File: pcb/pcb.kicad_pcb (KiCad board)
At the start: 2 copper layers, 130.9 x 223.4 mm, 44 parts, among them J1 GPS Module Breakout, J2 MicroSD Card Breakout, U1 XIAO-ESP32-C5-DIP, U10 XIAO-ESP32-C5-DIP, U11 XIAO-ESP32-C5-DIP, U12 XIAO-ESP32-C5-DIP, U13 XIAO-ESP32-C5-DIP, U14 XIAO-ESP32-C5-DIP, U15 XIAO-ESP32-C5-DIP, U16 XIAO-ESP32-C5-DIP, U17 ESP32-S3 DevKitC-1, U18 LD1117V33, U19 SN74HC125N, U2 XIAO-ESP32-C5-DIP, U20 SN74HC138N, U21 SN74HC138N, U3 XIAO-ESP32-C5-DIP, U4 XIAO-ESP32-C5-DIP, U5 XIAO-ESP32-C5-DIP, U6 XIAO-ESP32-C5-DIP, U7 XIAO-ESP32-C5-DIP, U8 XIAO-ESP32-C5-DIP, U9 XIAO-ESP32-C5-DIP

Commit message: implement more feedback from red :D
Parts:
- moved C2 5.35 mm to (68.4, 97.5), turned to 0 degrees
- moved R1 3.91 mm to (66.4, 120.5)
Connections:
- C2 pad 1: /CS 00 -> Net-(J2-Pin_6)
- J2 pad 6: /CS 00 -> Net-(J2-Pin_6)
- R1 pad 1: /CS 00 -> Net-(J2-Pin_6)
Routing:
- net +5V: track 0.00 -> 365.9 mm
- net GND: track 0.00 -> 365.6 mm
- net /MOSI: track 0.00 -> 240.4 mm
- net /MISO: track 0.00 -> 235.9 mm
- net /SCK: track 0.00 -> 232.9 mm
- net /CS 01: track 0.00 -> 145.0 mm
- net /CS 02: track 0.00 -> 117.6 mm
- net /CS 08: track 0.00 -> 110.9 mm
- net /CS 03: track 0.00 -> 91.0 mm
- net /CS 07: track 0.00 -> 90.7 mm
- net /CS 06: track 0.00 -> 67.2 mm
- net /CS 04: track 0.00 -> 63.7 mm
- net /CS 05: track 0.00 -> 55.5 mm
- net Net-(U18-VO): track 0.00 -> 41.9 mm
- net /CS 00: track 0.00 -> 37.5 mm
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- added copper zone on F.Cu, net GND

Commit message: Reroute the board!
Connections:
- C2 pad 1: Net-(J2-Pin_6) -> +3.3V
- C2 pad 2: Net-(U18-VO) -> GND
- C3 pad 2: Net-(U18-VO) -> +3.3V
- J2 pad 1: Net-(J2-Pin_1) -> /CS 00
- J2 pad 6: Net-(J2-Pin_6) -> +3.3V
- R1 pad 1: Net-(J2-Pin_6) -> +3.3V
- U18 pad 2: Net-(U18-VO) -> +3.3V
- U19 pad 11: Net-(J2-Pin_1) -> unconnected-(U19-4Y-Pad11)
- U19 pad 12: /CS 00 -> GND
- U19 pad 14: Net-(U18-VO) -> +3.3V
- U20 pad 16: +5V -> +3.3V
- U20 pad 6: +5V -> +3.3V
- U21 pad 16: +5V -> +3.3V
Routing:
- net /MOSI: track 240.4 -> 604.1 mm, vias 0 -> 5
- net /MISO: track 235.9 -> 582.3 mm, vias 0 -> 3
- net /SCK: track 232.9 -> 578.6 mm, vias 0 -> 3
- net +5V: track 365.9 -> 645.8 mm
- net GND: track 365.6 -> 515.0 mm
- net /CS 09: track 0.00 -> 141.6 mm
- net +3.3V: track 0.00 -> 138.3 mm, vias 0 -> 3
- net /GPS_TX: track 0.00 -> 132.3 mm
- net /GPS_RX: track 0.00 -> 126.1 mm
- net /CS 15: track 0.00 -> 119.7 mm
- net /CS 10: track 0.00 -> 112.0 mm
- net /CS 11: track 0.00 -> 90.9 mm
- net /CS 16: track 0.00 -> 84.7 mm
- net /CS 00: track 37.5 -> 115.6 mm
- net /CS Addr 1: track 0.00 -> 77.4 mm
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
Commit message: Add brownout protection
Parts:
- added C4: 47uF, Capacitor_THT:C_Disc_D5.0mm_W2.5mm_P2.50mm, F.Cu at (76.5, 17.0)
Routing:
- net +5V: track 645.8 -> 650.1 mm

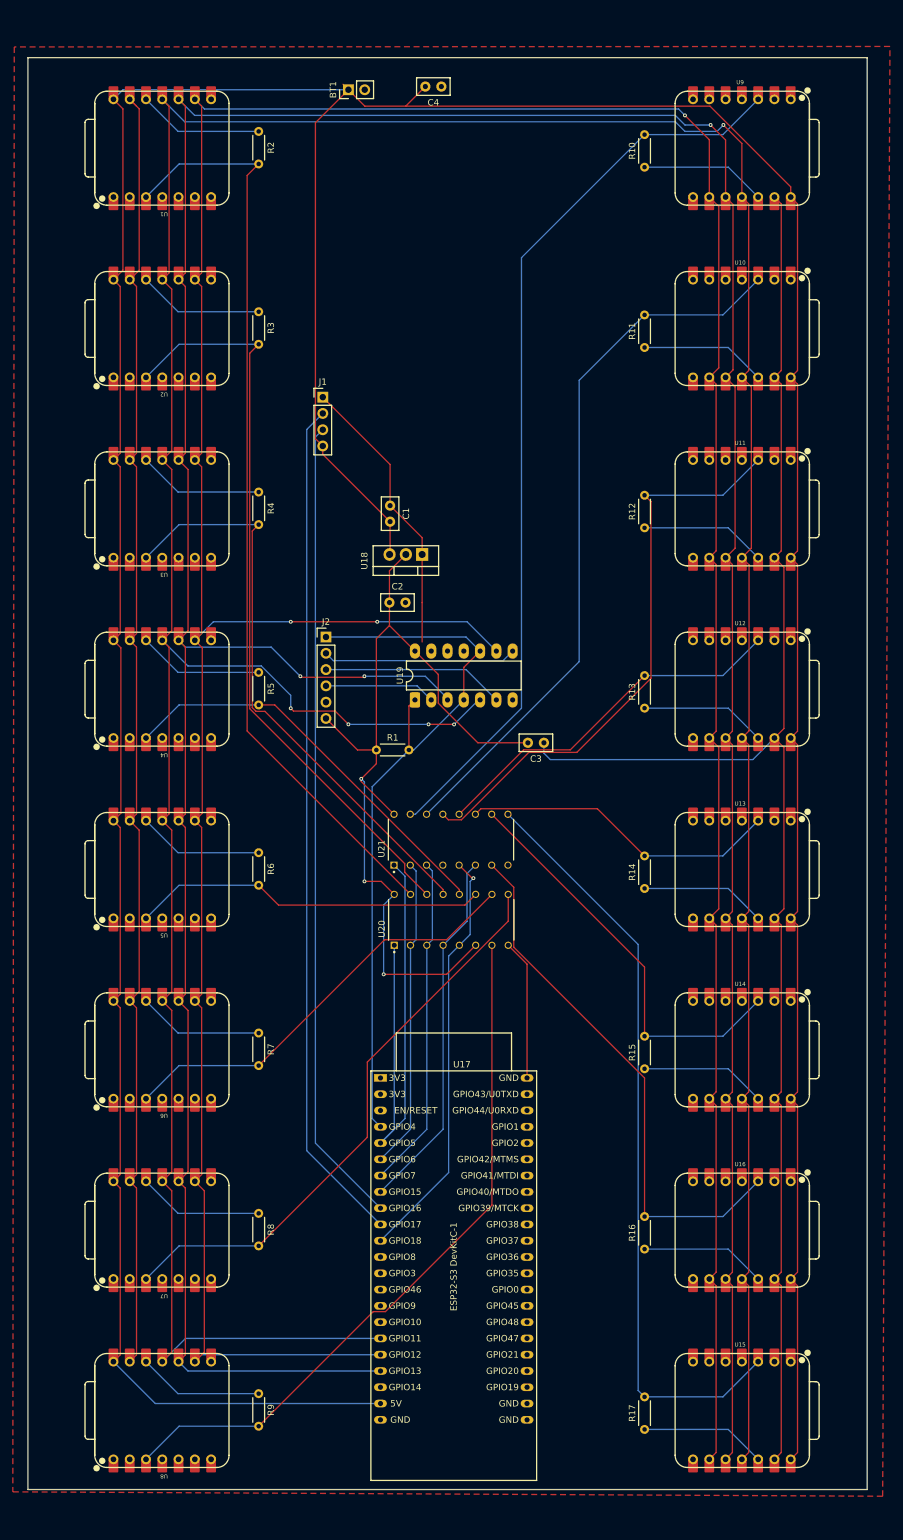
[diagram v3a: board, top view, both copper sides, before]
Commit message: 0.3mm power net
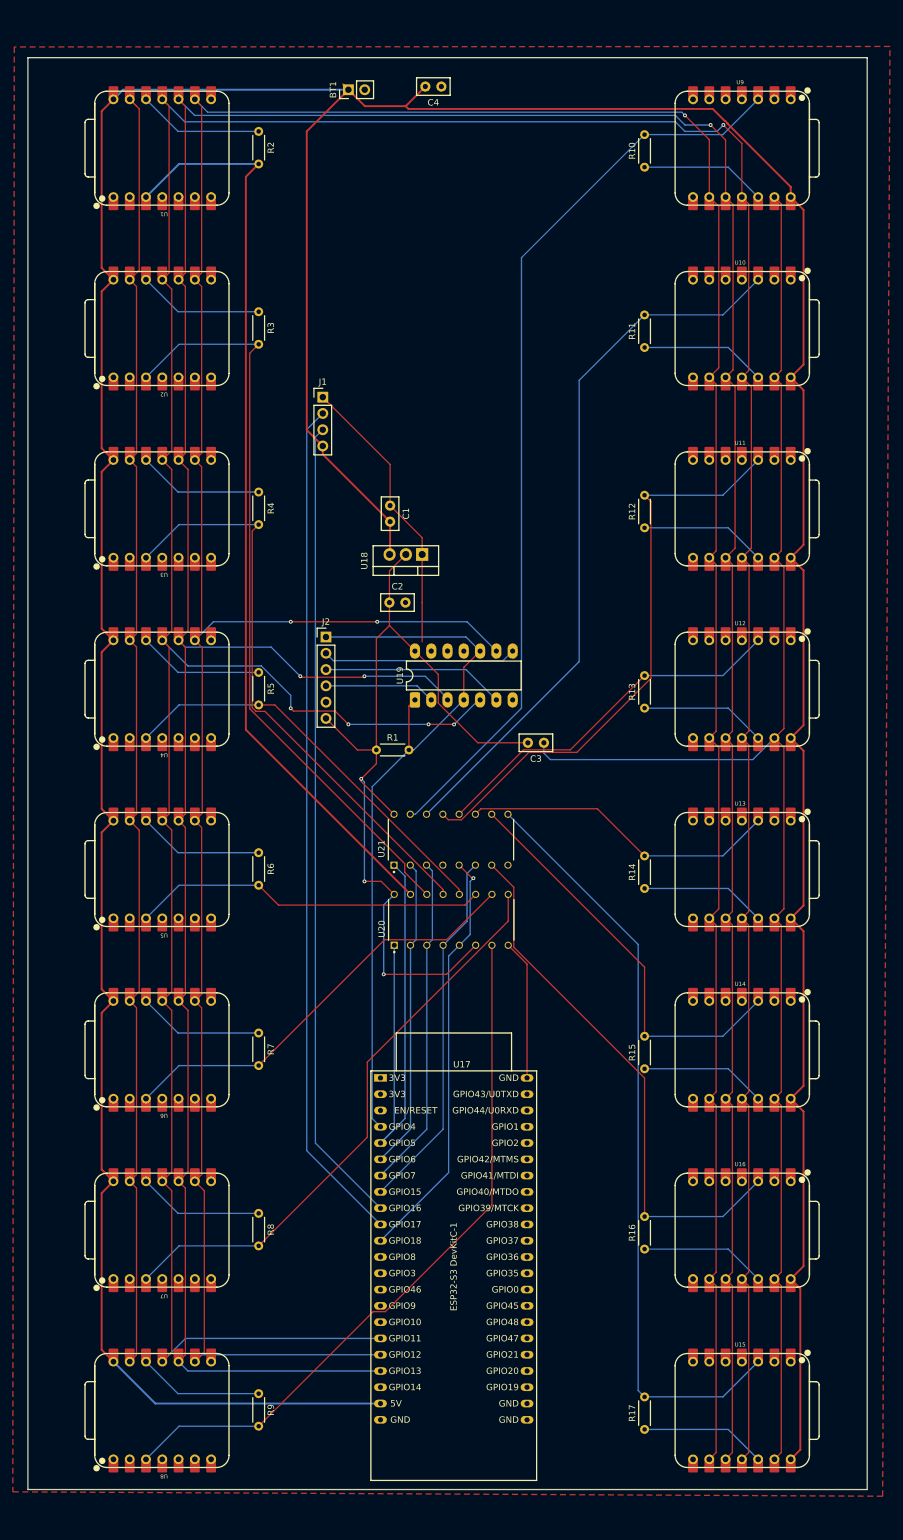
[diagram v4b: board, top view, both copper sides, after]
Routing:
- net +5V: track 650.1 -> 660.4 mm

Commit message: Thicker tracks, remove redundant ground lines, mounting holes
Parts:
- added ?: MountingHole, MountingHole:MountingHole_3.2mm_M3, F.Cu at (18.0, 18.0)
- added ?: MountingHole, MountingHole:MountingHole_3.2mm_M3, F.Cu at (138.0, 230.0)
- added ?: MountingHole, MountingHole:MountingHole_3.2mm_M3, F.Cu at (18.0, 230.0)
- added ?: MountingHole, MountingHole:MountingHole_3.2mm_M3, F.Cu at (138.0, 18.0)
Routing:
- net GND: track 515.0 -> 0.08 mm
- net +5V: track 660.4 -> 706.3 mm
- net +3.3V: track 138.3 -> 150.0 mm
- net /CS 01: track 145.1 -> 145.8 mm
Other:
- board size 130.9 x 223.4 mm -> 132 x 224 mm

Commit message: Fix 15/16 ordering
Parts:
- gave numbers to parts that had none: 4
- renumbered R2 to R1, R11 to R10, R12 to R11, R13 to R12, R14 to R13, R15 to R14, R16 to R15, R17 to R16, R1 to R17, R3 to R2, R4 to R3, R5 to R4, R6 to R5, R7 to R6, R8 to R7, R9 to R8, R10 to R9, U16 to U15, U15 to U16
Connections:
- R15 pad 2: /CS 16 -> /CS 15
- R16 pad 2: /CS 15 -> /CS 16
- U15 pad 3: /CS 16 -> /CS 15
- U16 pad 3: /CS 15 -> /CS 16
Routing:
- net /CS 16: track 84.7 -> 114.2 mm
- net /CS 15: track 119.7 -> 92.7 mm

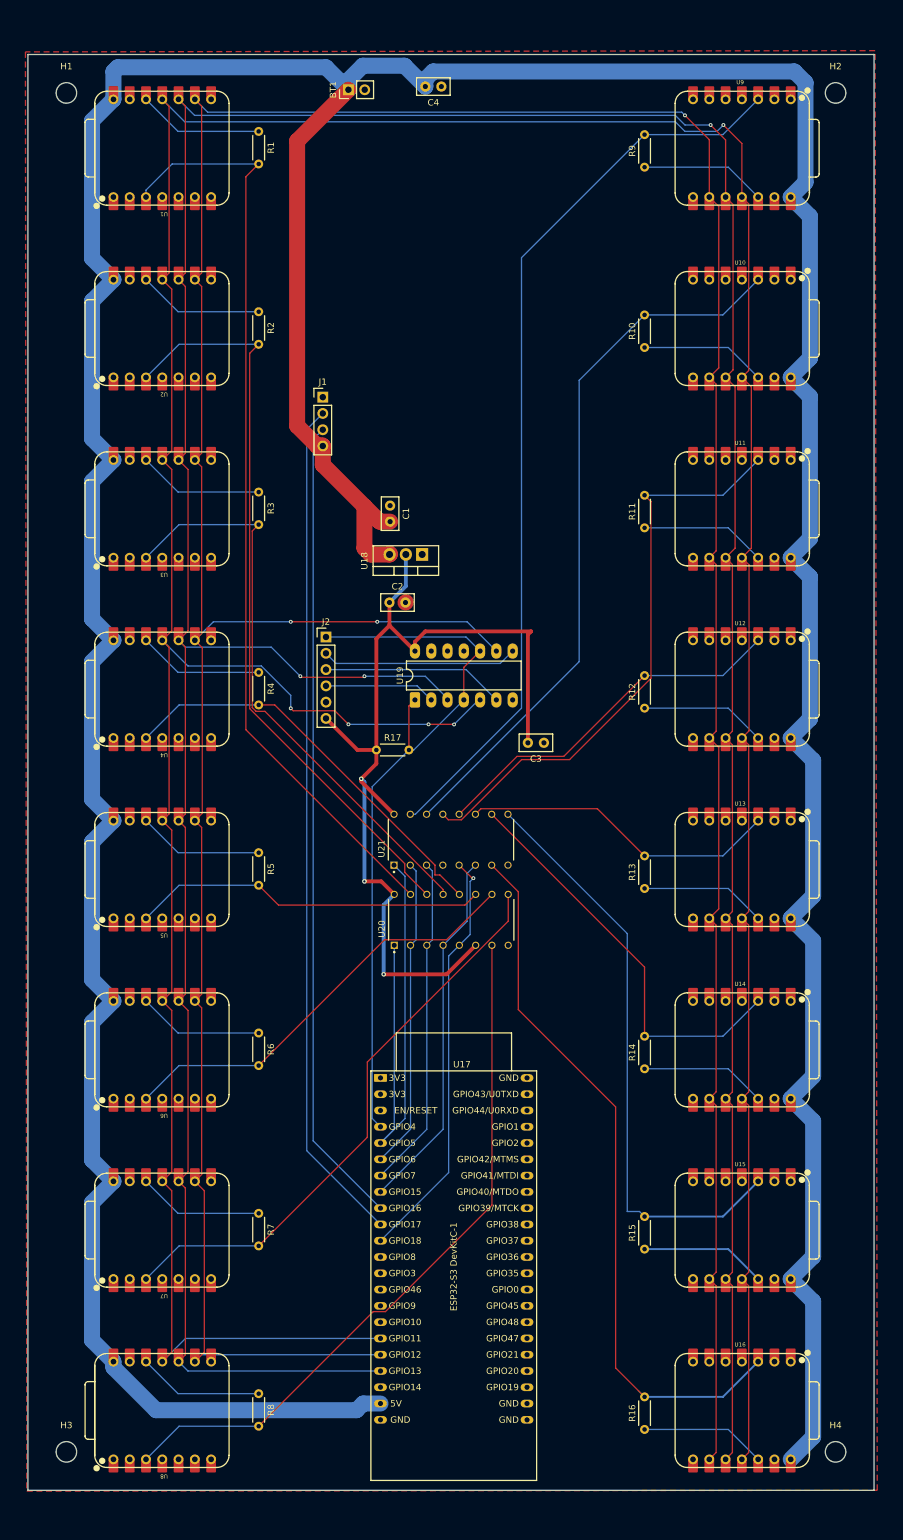
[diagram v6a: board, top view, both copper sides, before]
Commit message: add exhaust fan power
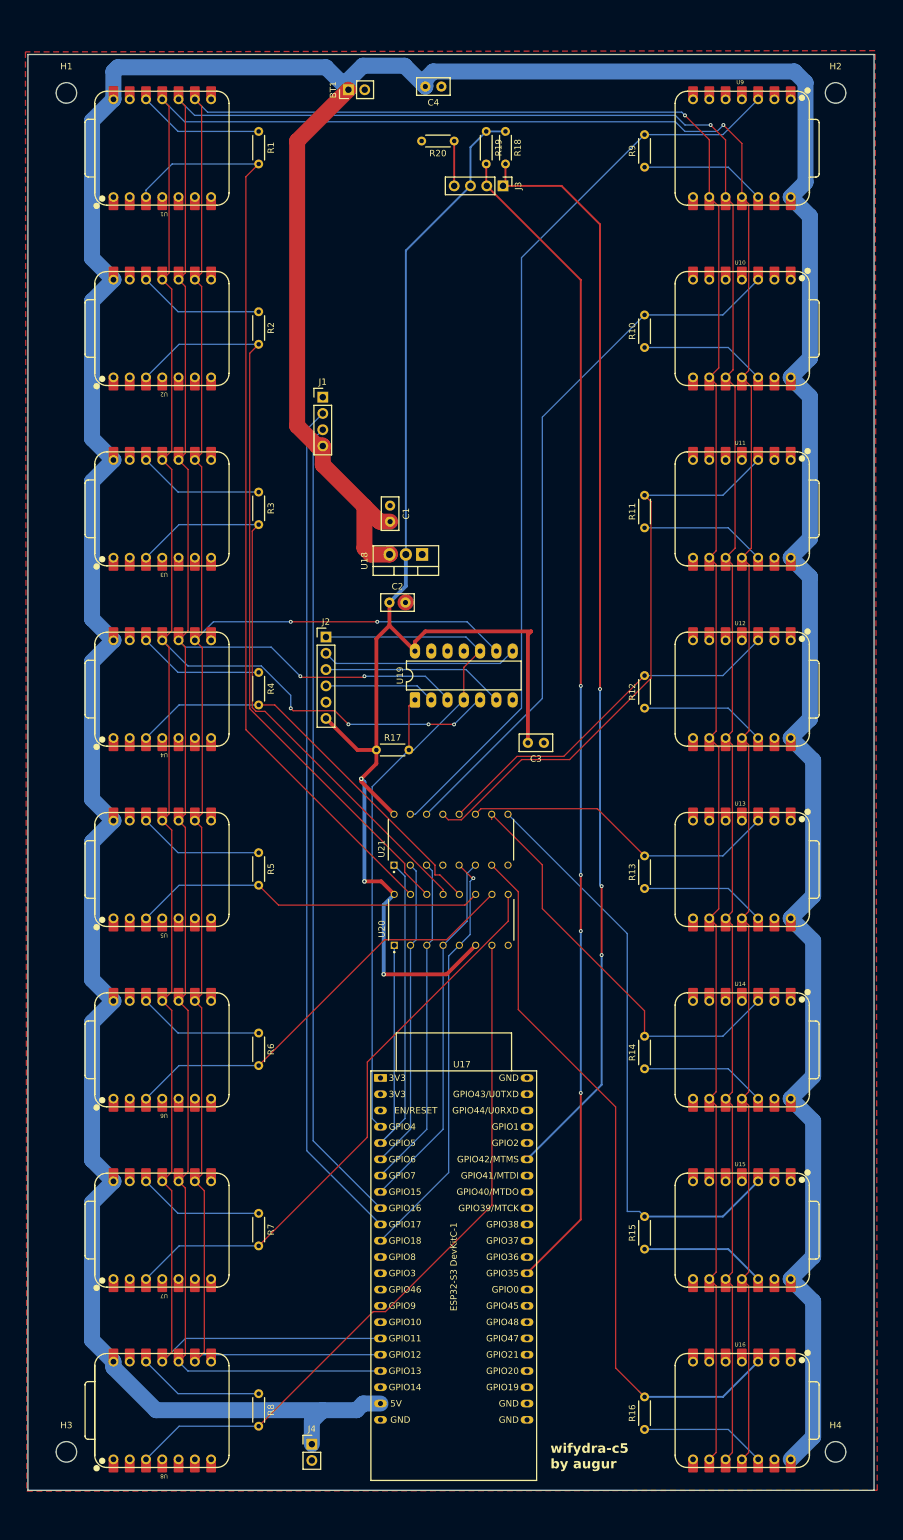
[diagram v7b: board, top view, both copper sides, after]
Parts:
- added J3: I2C Display, Connector_PinHeader_2.54mm:PinHeader_1x04_P2.54mm_Vertical, F.Cu at (86.1, 32.5)
- added J4: Exhaust Fan, Connector_PinHeader_2.54mm:PinHeader_1x02_P2.54mm_Vertical, F.Cu at (56.3, 228.8)
- added R18: 10k, Resistor_THT:R_Axial_DIN0204_L3.6mm_D1.6mm_P5.08mm_Horizontal, F.Cu at (86.5, 24.0)
- added R19: 10k, Resistor_THT:R_Axial_DIN0204_L3.6mm_D1.6mm_P5.08mm_Horizontal, F.Cu at (83.5, 24.0)
- added R20: 100nf, Resistor_THT:R_Axial_DIN0204_L3.6mm_D1.6mm_P5.08mm_Horizontal, F.Cu at (78.5, 25.5)
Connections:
- U17 pad 32: unconnected-(U17-GPIO38-Pad32) -> /SCL
- U17 pad 39: unconnected-(U17-GPIO47-Pad39) -> /SDA
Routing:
- net /SCL: track 0.00 -> 182.6 mm, vias 0 -> 4
- net /SDA: track 0.00 -> 172.0 mm, vias 0 -> 3
- net +3.3V: track 150.0 -> 224.2 mm
- net Net-(J3-Pin_4): track 0.00 -> 7.00 mm
- net +5V: track 706.3 -> 712.3 mm
- net /CS 14: track 64.5 -> 65.3 mm
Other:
- board text added: "wifydra-c5 by augur"

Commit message: Migrate to two copper fills, one for power, one for ground
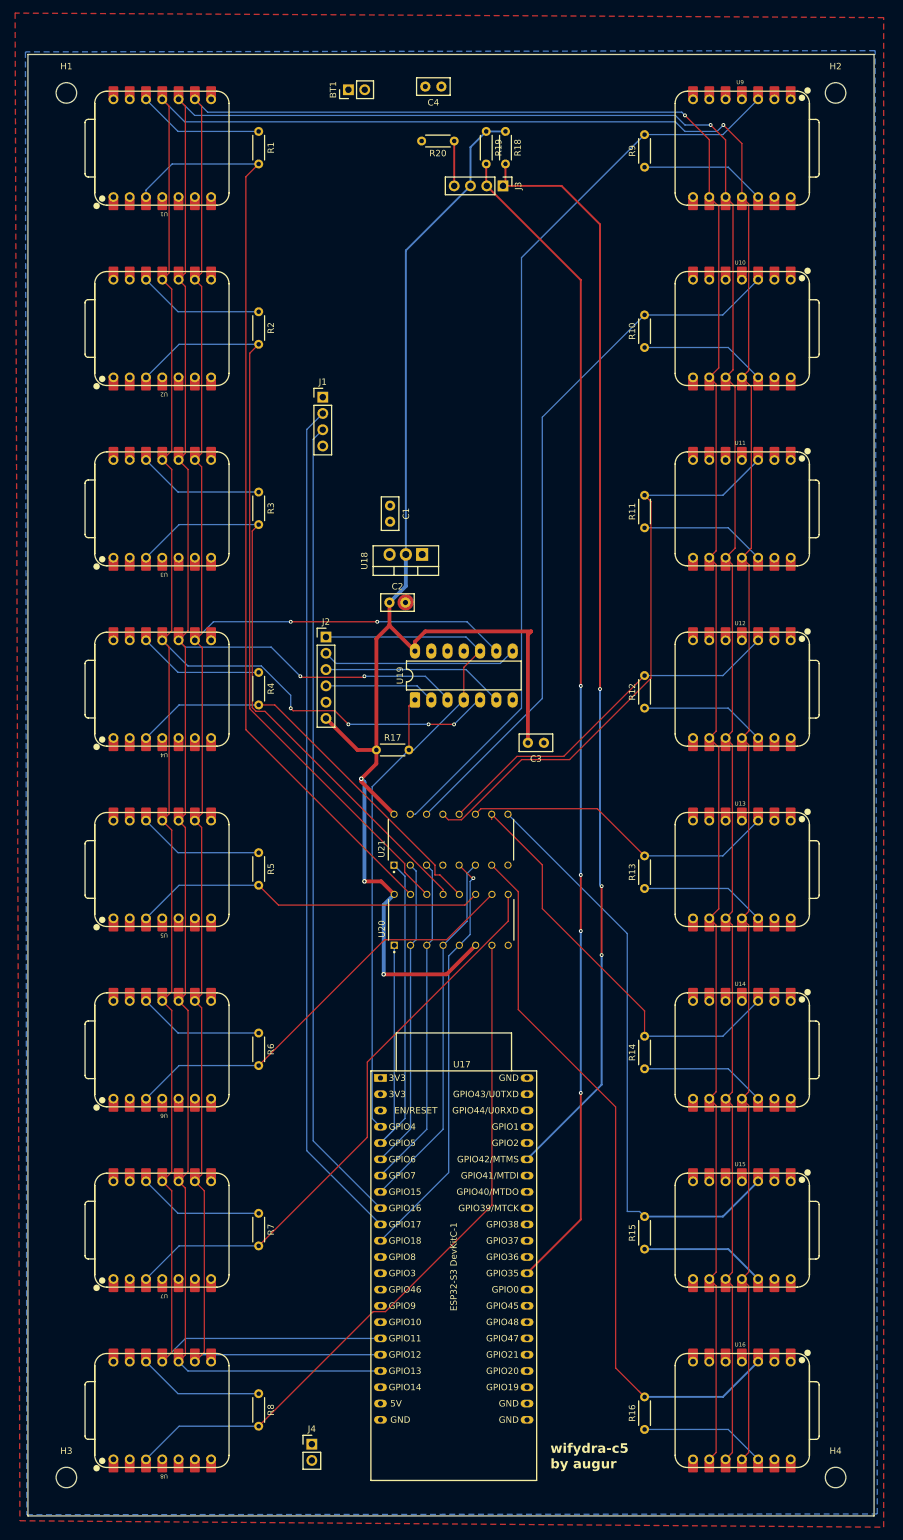
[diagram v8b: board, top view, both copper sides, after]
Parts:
- moved H3 4.00 mm to (18.0, 234.0)
- moved H4 4.00 mm to (138.0, 234.0)
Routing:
- net +5V: track 712.3 -> 0.00 mm
- added copper zone on F.Cu, net +5V
- added copper zone on B.Cu, net GND
- removed copper zone on F.Cu, net GND
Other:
- board size 132 x 224 mm -> 132 x 228 mm
